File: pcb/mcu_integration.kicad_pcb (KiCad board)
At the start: 4 copper layers, 90.2 x 95.9 mm, 82 parts, among them IC1 TL7660IDGKR, IC10 AD844_OPAMP_MEL, IC3 FOD814_OPTO_NOSHD, IC4 UA78M33CDCYG3, IC5 FOD814_OPTO_MEL, IC6 AD844_OPAMP_AL, IC7 FOD814_OPTO_AL, IC8 AD844_OPAMP_NOSHD, J1 Micro_SD_Card, J2 ESQ-126-39-L-D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

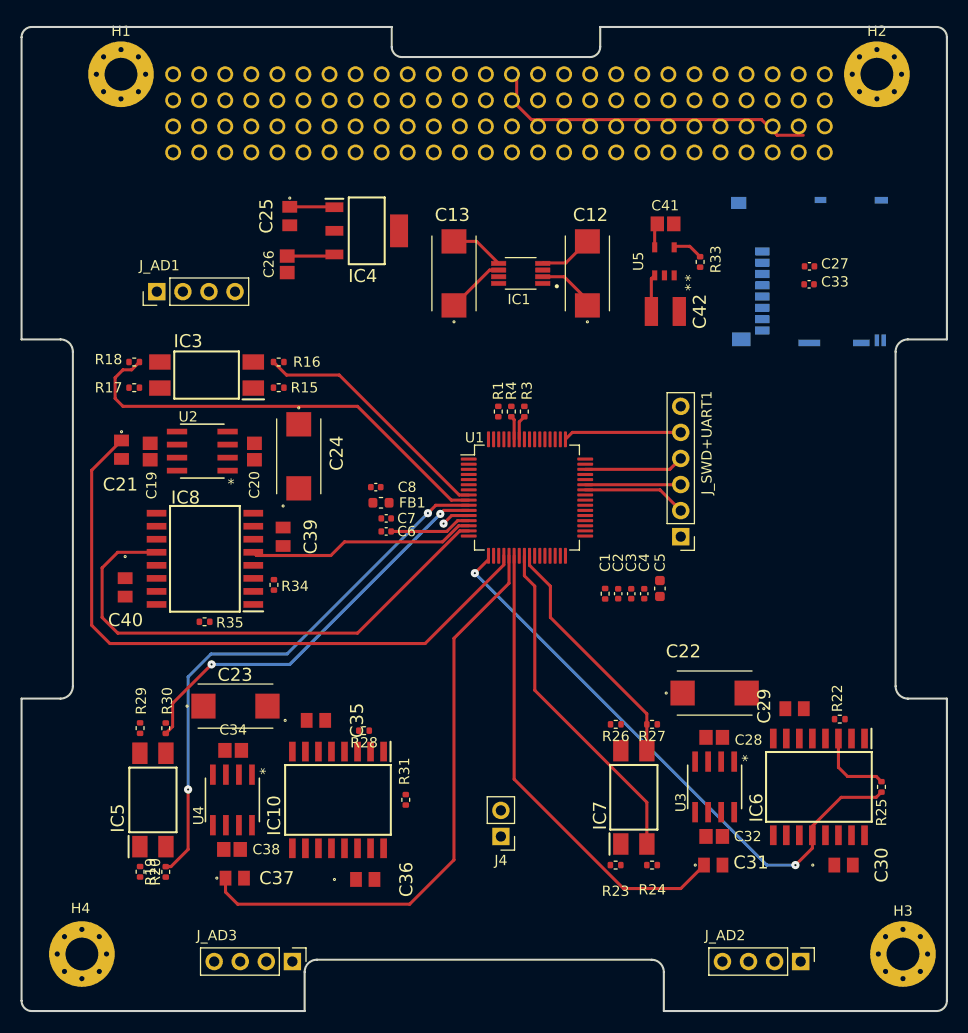
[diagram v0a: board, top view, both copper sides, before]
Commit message: SD card change
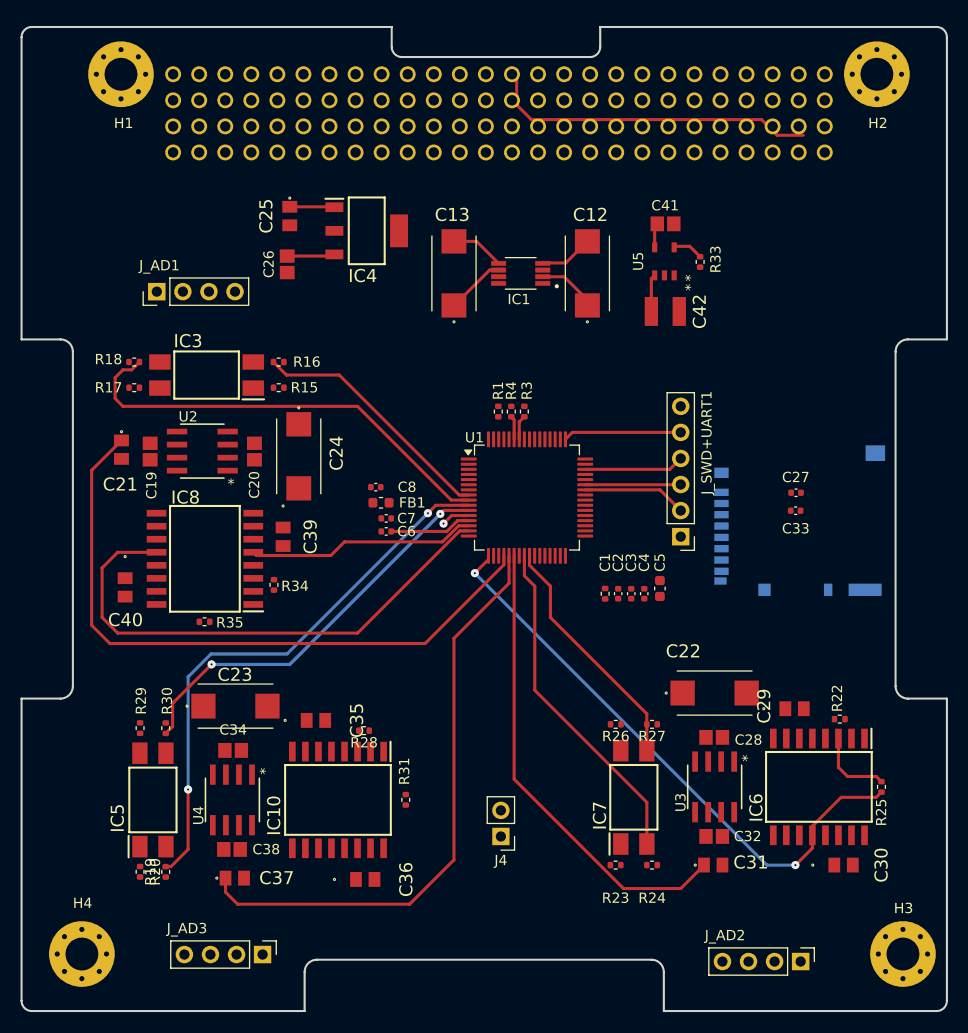
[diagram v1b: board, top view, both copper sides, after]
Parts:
- removed J1: Micro_SD_Card, capstone:22017781
- added J5: DM3BT-DSF-PEJS, capstone:DM3BT_DSF_PEJS, B.Cu at (168.6, 99.7)
- moved C27 22.1 mm to (168.0, 97.0)
- moved C33 22.1 mm to (168.0, 98.8)
- moved J_AD3 2.98 mm to (116.0, 142.0)

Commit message: Routed all connections
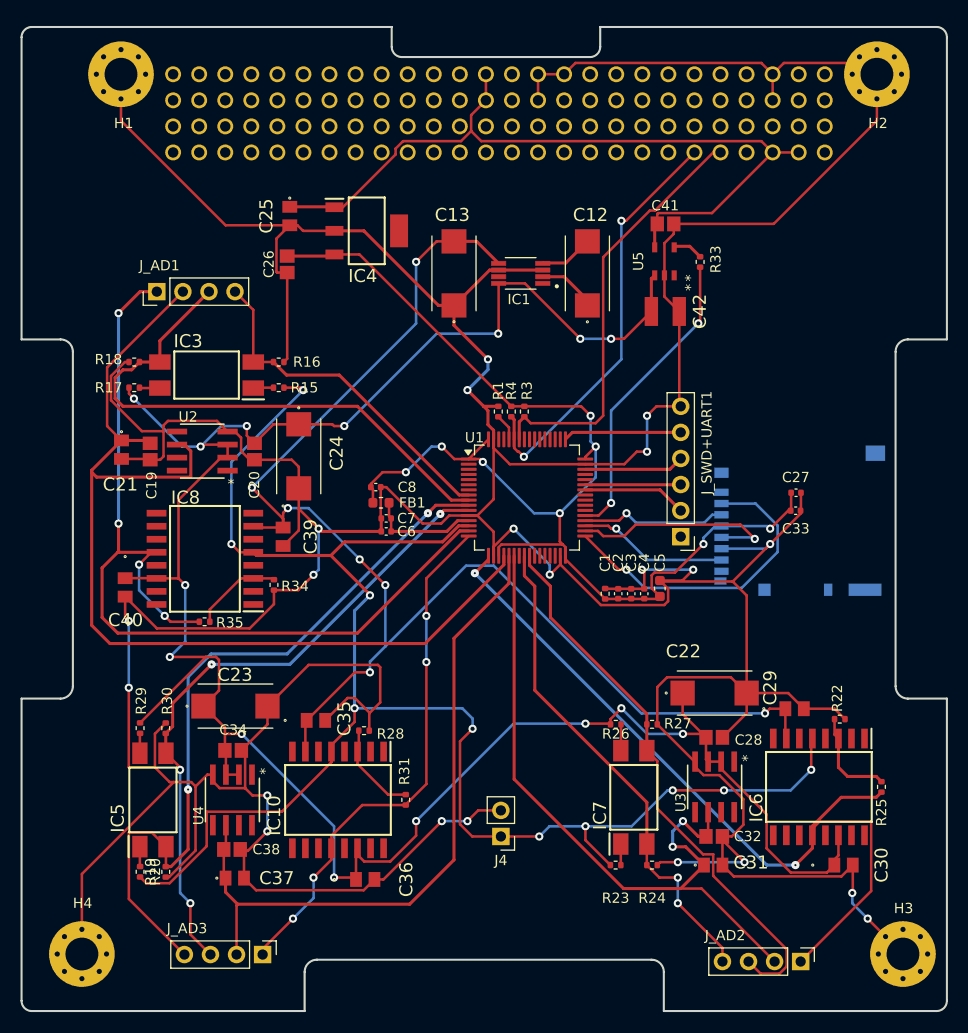
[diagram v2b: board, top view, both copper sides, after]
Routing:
- net GND: track 8.56 -> 608.5 mm, vias 1 -> 21
- net +5V: track 3.65 -> 230.3 mm, vias 0 -> 15
- net ADC1_IN0_SINE: track 22.3 -> 161.7 mm, vias 0 -> 10
- net -5V Output: track 5.24 -> 132.9 mm, vias 0 -> 7
- net 3.3V Output: track 4.67 -> 119.9 mm, vias 0 -> 8
- net ADC1_IN2_OPAMP_MEL: track 0.00 -> 51.7 mm, vias 0 -> 4
- net ADC1_IN1_OPAMP_NOSHD: track 51.2 -> 91.0 mm, vias 0 -> 4
- net OBC_I2C_SCL: track 2.40 -> 41.8 mm
- net OBC_I2C_SDA: track 2.31 -> 41.3 mm, vias 0 -> 2
- net +5V_EXT: track 38.4 -> 77.1 mm
- net ADC1_IN4_VREF_NOSHD: track 64.2 -> 99.2 mm
- net ADC1_IN15_OPTO_E_AL: track 23.7 -> 55.5 mm
- net /SPI2_CS_NSS: track 0.00 -> 31.2 mm, vias 0 -> 1
- net MOSFET_CONTROL: track 0.00 -> 29.6 mm, vias 0 -> 2
- net ADC1_IN6_VREF_AL: track 45.6 -> 69.7 mm, vias 0 -> 2
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
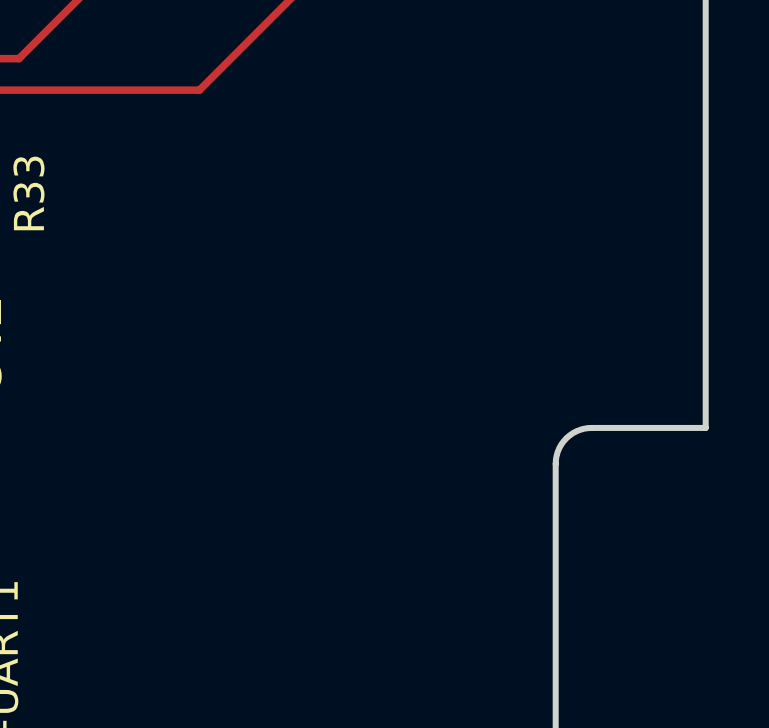
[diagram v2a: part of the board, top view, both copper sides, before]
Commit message: Added LM35 Temp Sensor
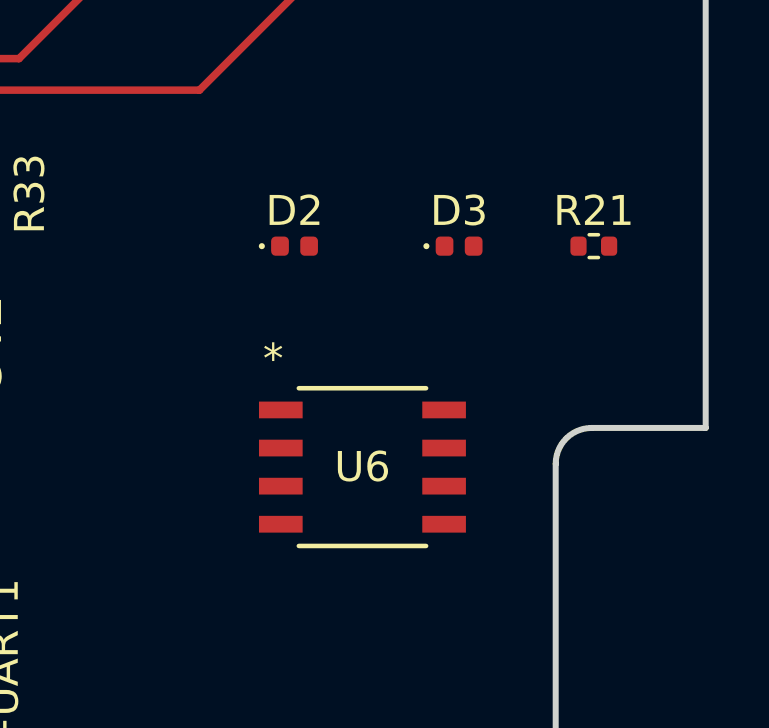
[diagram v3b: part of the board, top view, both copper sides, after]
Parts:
- added D2: 1N914, Diode_SMD:D_0402_1005Metric, F.Cu at (169.0, 76.0)
- added D3: 1N914, Diode_SMD:D_0402_1005Metric, F.Cu at (174.5, 76.0)
- added R21: 18K, Resistor_SMD:R_0402_1005Metric, F.Cu at (179.0, 76.0)
- added U6: LM35DM, capstone:LM35DM, F.Cu at (171.3, 83.4)

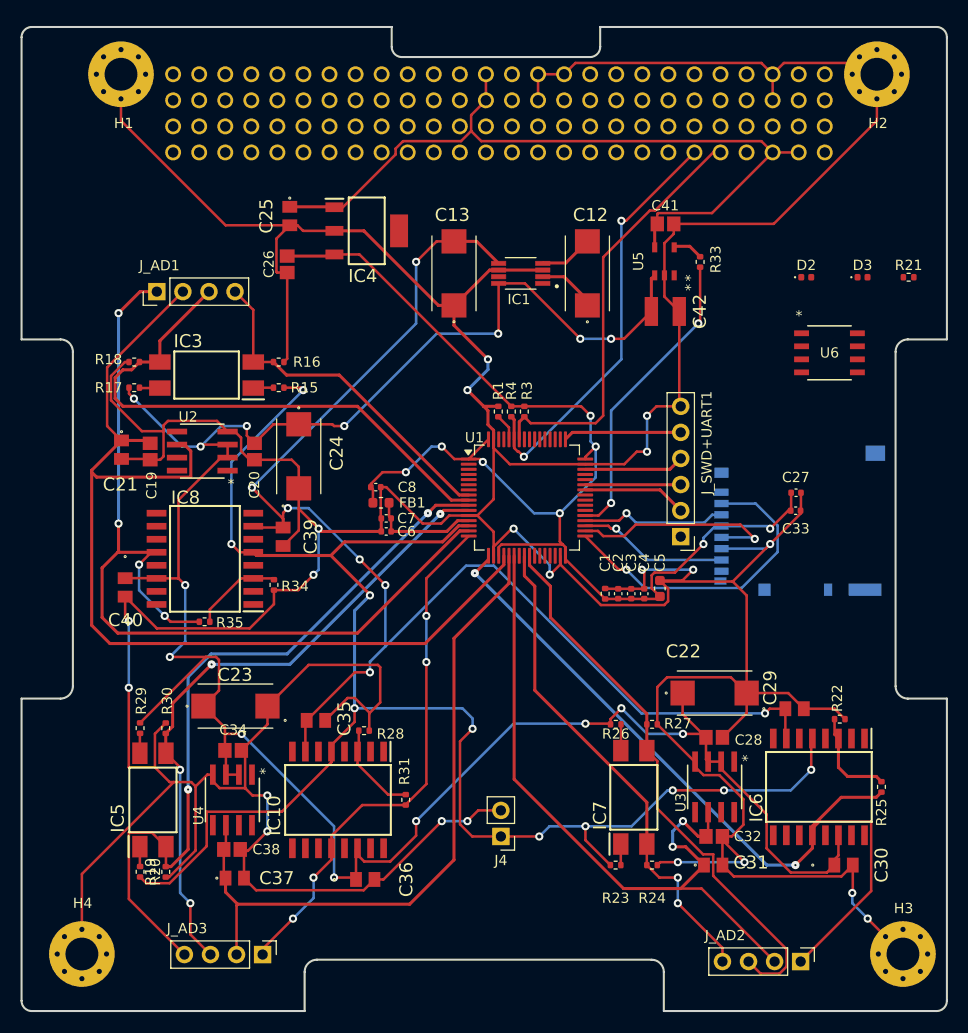
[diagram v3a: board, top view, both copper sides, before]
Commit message: Added GND and PWR planes
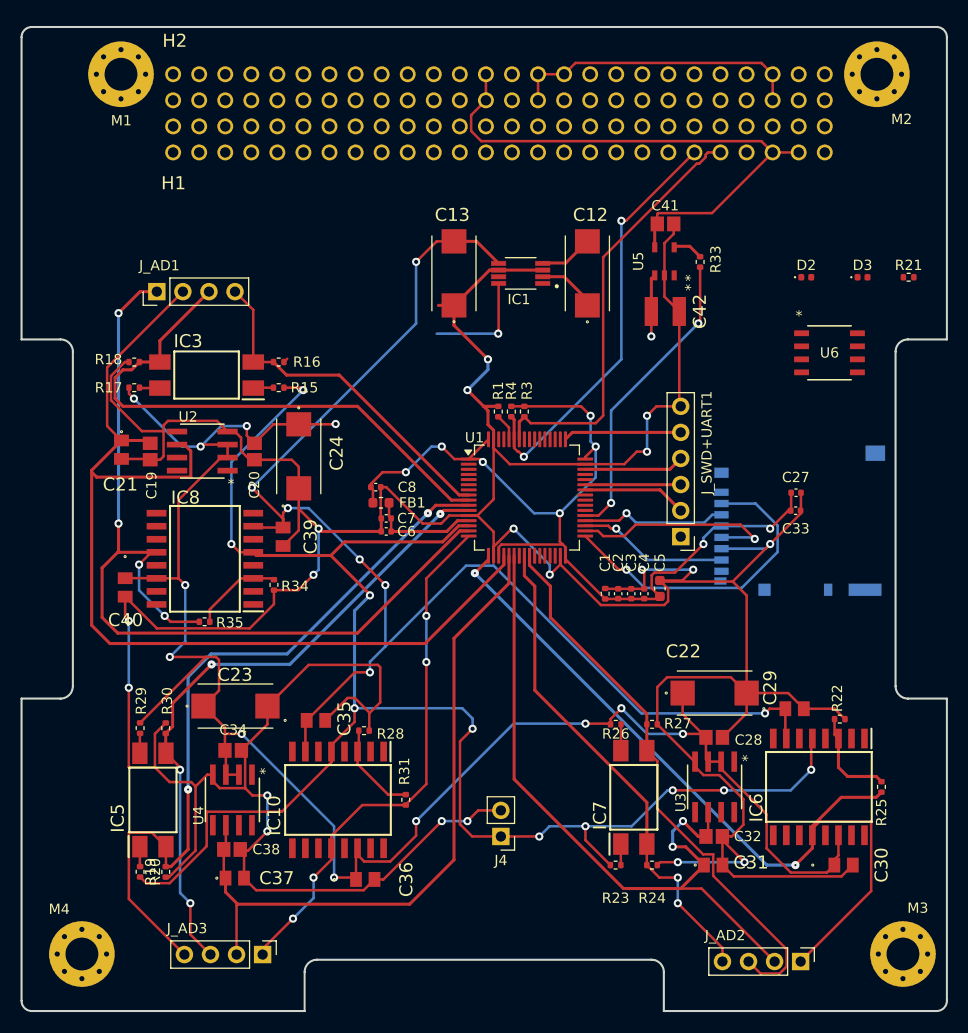
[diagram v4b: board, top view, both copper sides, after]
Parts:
- removed C25: 0.33u, capstone:C0805
- removed C26: 0.1u, capstone:CAPC220145_88N_KEM-0.1u
- removed IC4: UA78M33CDCYG3, capstone:SOT230P700X180-4N
- renumbered J2 to H1, J3 to H2, H1 to M1, H2 to M2, H3 to M3, H4 to M4
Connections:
- H2 pad 27: unconnected-(J3-Pad27) -> 3.3V Output
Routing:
- net GND: track 608.5 -> 481.8 mm, vias 21 -> 19
- net +5V: track 230.3 -> 200.9 mm, vias 15 -> 14
- net 3.3V Output: track 119.9 -> 91.8 mm
- net +5V_EXT: track 77.1 -> 56.0 mm
- added copper zone on In2.Cu, net +5V
- added copper zone on In1.Cu, net GND
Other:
- outline, holes or cut-outs redrawn

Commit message: Connected GND connections to GND plane
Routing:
- net GND: track 481.8 -> 174.1 mm, vias 19 -> 31
- net ADC1_IN9_VREG_AL: track 0.00 -> 62.8 mm
- net 3.3V Output: track 91.8 -> 120.8 mm, vias 8 -> 9
- net Net-(D2-K): track 0.00 -> 7.19 mm
- net +5V: track 200.9 -> 196.9 mm, vias 14 -> 15

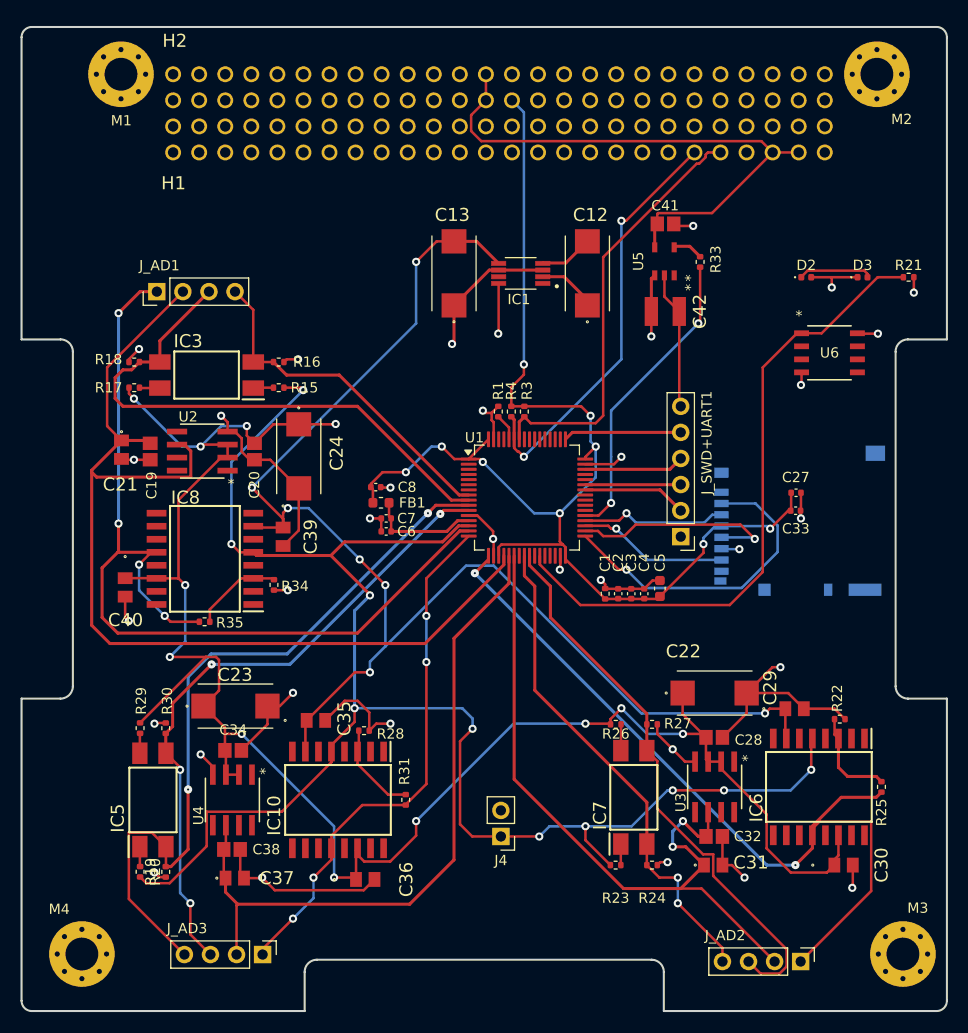
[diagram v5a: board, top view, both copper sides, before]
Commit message: Added +5v connections
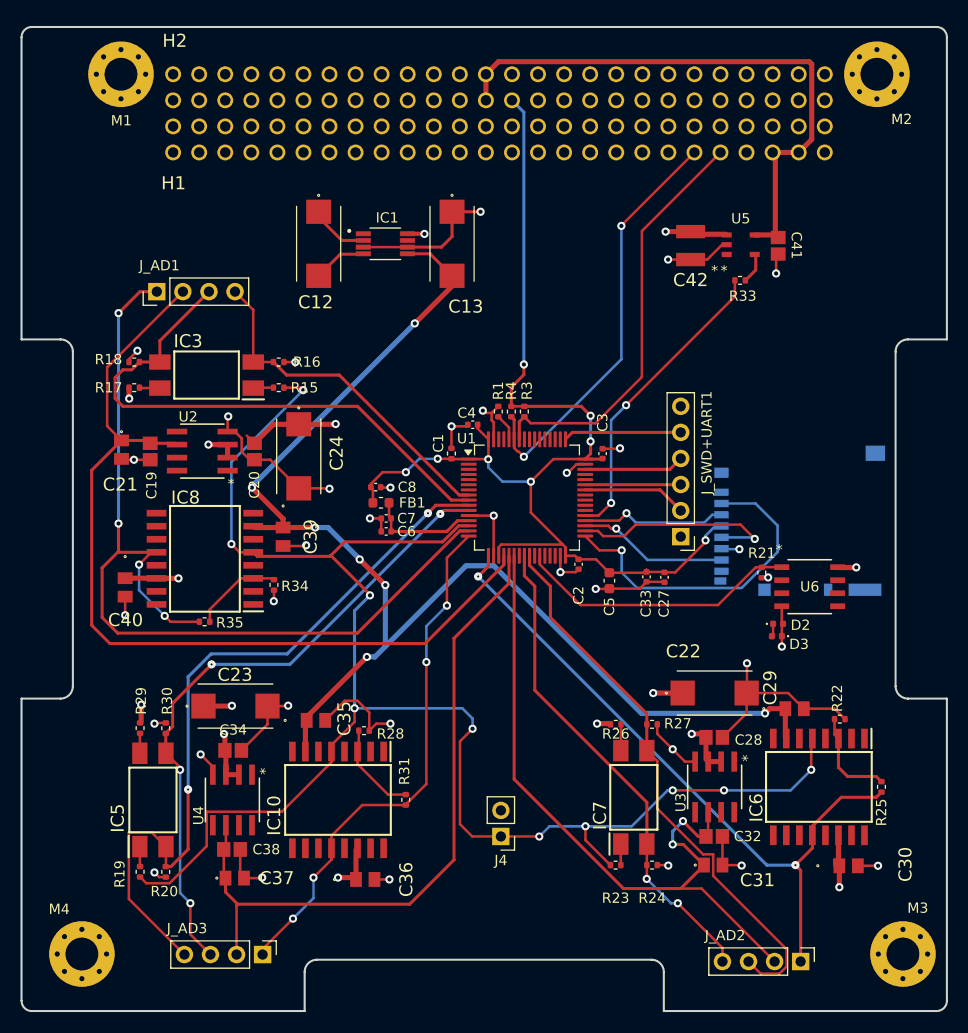
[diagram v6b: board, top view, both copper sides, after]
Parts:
- moved D3 36.0 mm to (166.2, 111.0), turned to 180 degrees
- moved D2 33.9 mm to (166.3, 109.8)
- moved R21 32.1 mm to (164.7, 104.8), turned to -90 degrees
- moved C12 26.3 mm to (121.5, 72.7), turned to -90 degrees
- moved C4 23.5 mm to (136.5, 90.4), turned to 180 degrees
- moved U6 22.9 mm to (169.4, 106.2)
- moved C1 20.3 mm to (134.4, 93.2)
- moved C33 15.9 mm to (153.4, 105.2), turned to -90 degrees
- moved C27 15.2 mm to (155.2, 105.2), turned to -90 degrees
- moved C3 13.9 mm to (149.2, 93.2)
- moved IC1 13.5 mm to (128.0, 72.7), turned to 0 degrees
- moved C41 11.2 mm to (166.3, 72.9), turned to -90 degrees
- moved U5 7.61 mm to (162.6, 72.8), turned to 0 degrees
- moved C42 6.88 mm to (157.7, 72.9), turned to -90 degrees
- moved C5 4.98 mm to (149.8, 105.6), turned to -90 degrees
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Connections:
- net Net-(D2-K) renamed DIODE_NET
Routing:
- net +5V: track 196.9 -> 60.7 mm
- net ADC1_IN9_VREG_AL: track 62.8 -> 27.6 mm
- net GND: track 174.1 -> 152.1 mm, vias 31 -> 35
- net ADC1_IN3_OPAMP_AL: track 81.0 -> 67.8 mm
- net 3.3V Output: track 120.8 -> 109.6 mm, vias 9 -> 8
- net ADC1_IN4_VREF_NOSHD: track 99.2 -> 88.6 mm
- net -5V Output: track 132.9 -> 125.6 mm
- net DIODE_NET: track 7.19 -> 1.41 mm
- net /SPI2_CS_NSS: track 31.2 -> 32.5 mm
- net +5V_EXT: track 56.0 -> 57.1 mm
- net OBC_I2C_SCL: track 41.9 -> 41.0 mm
- net ADC1_IN14_OPTO_F_AL: track 48.6 -> 47.9 mm
